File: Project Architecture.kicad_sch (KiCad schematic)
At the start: 0 parts

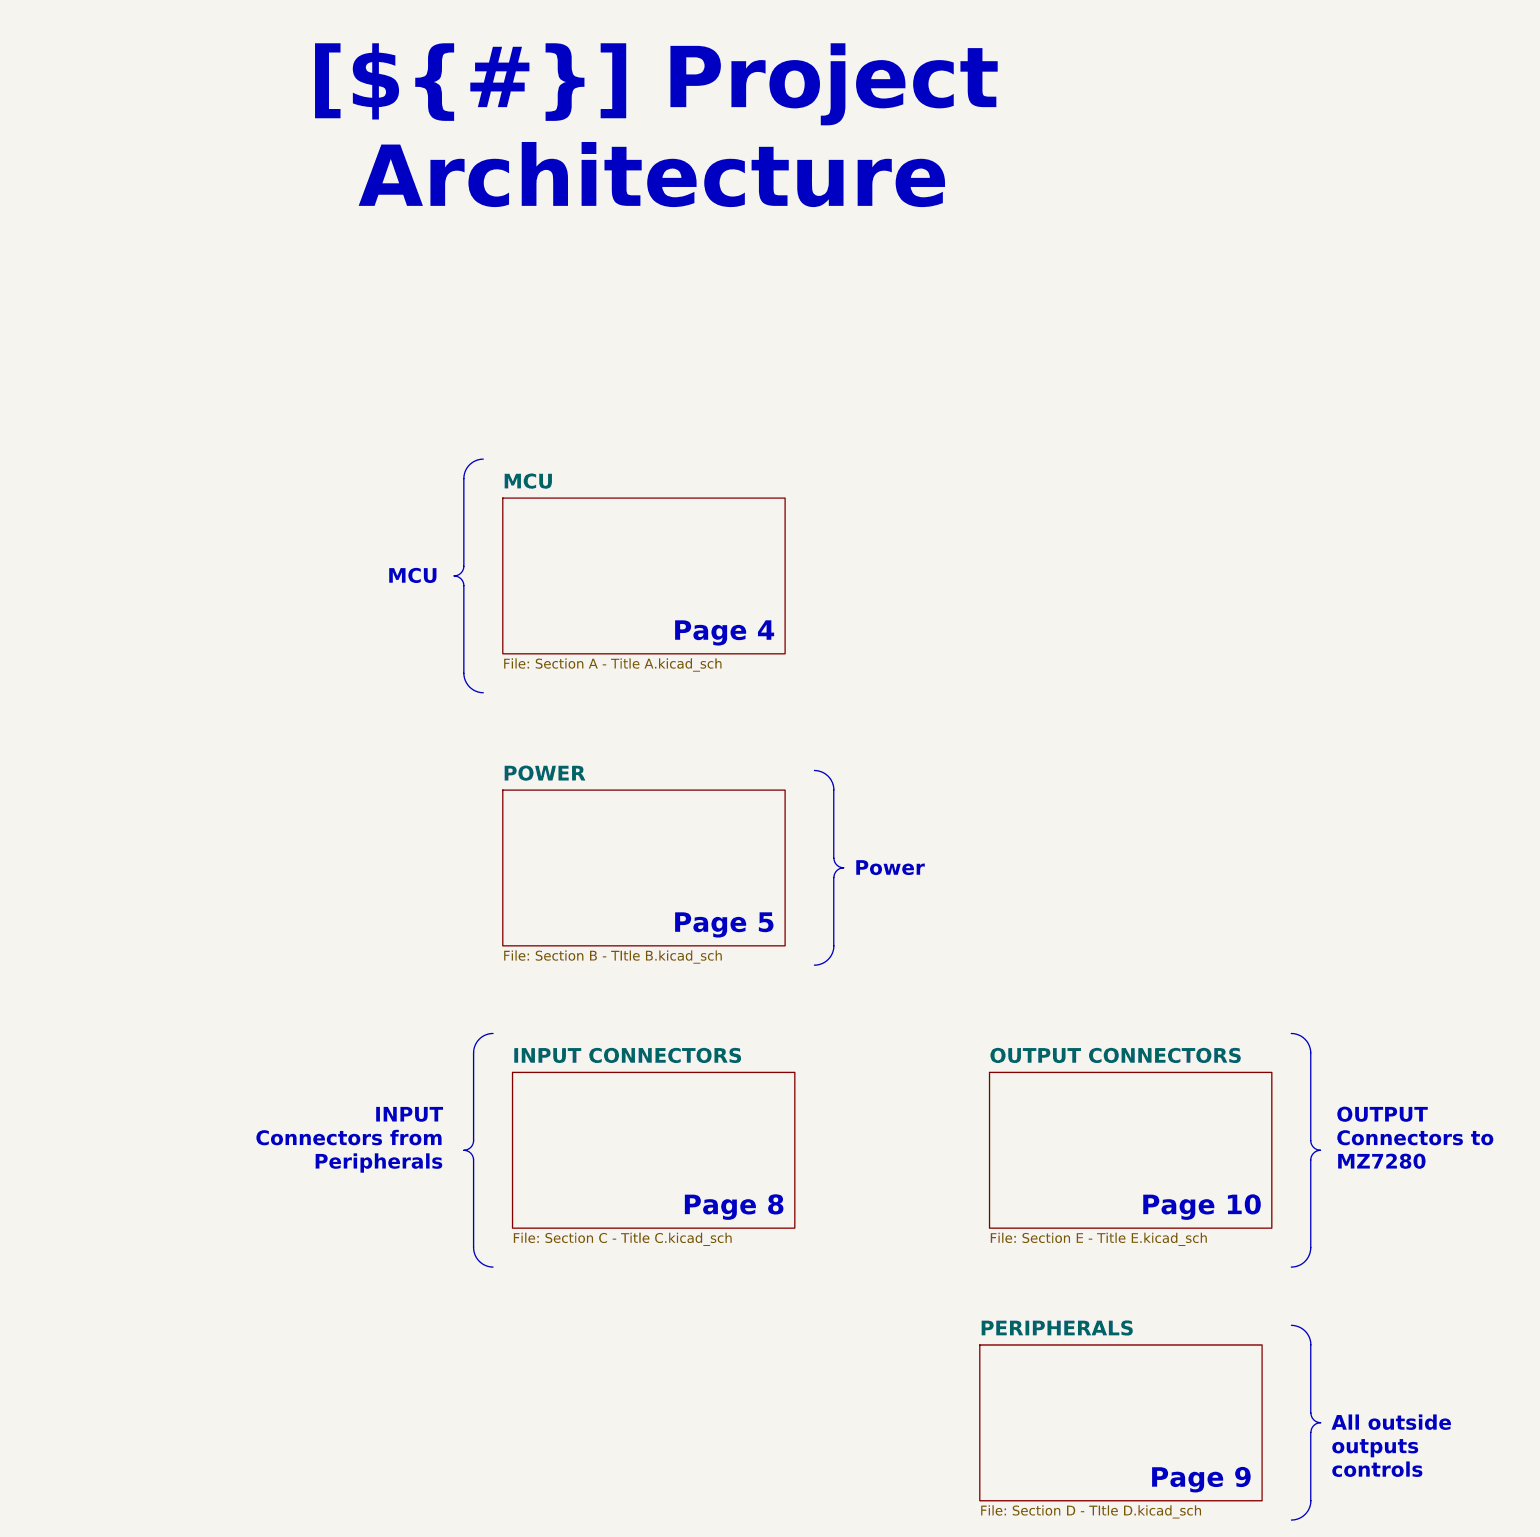
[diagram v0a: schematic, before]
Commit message: [SCHEMATICS] Ajout de convertisseur + autres
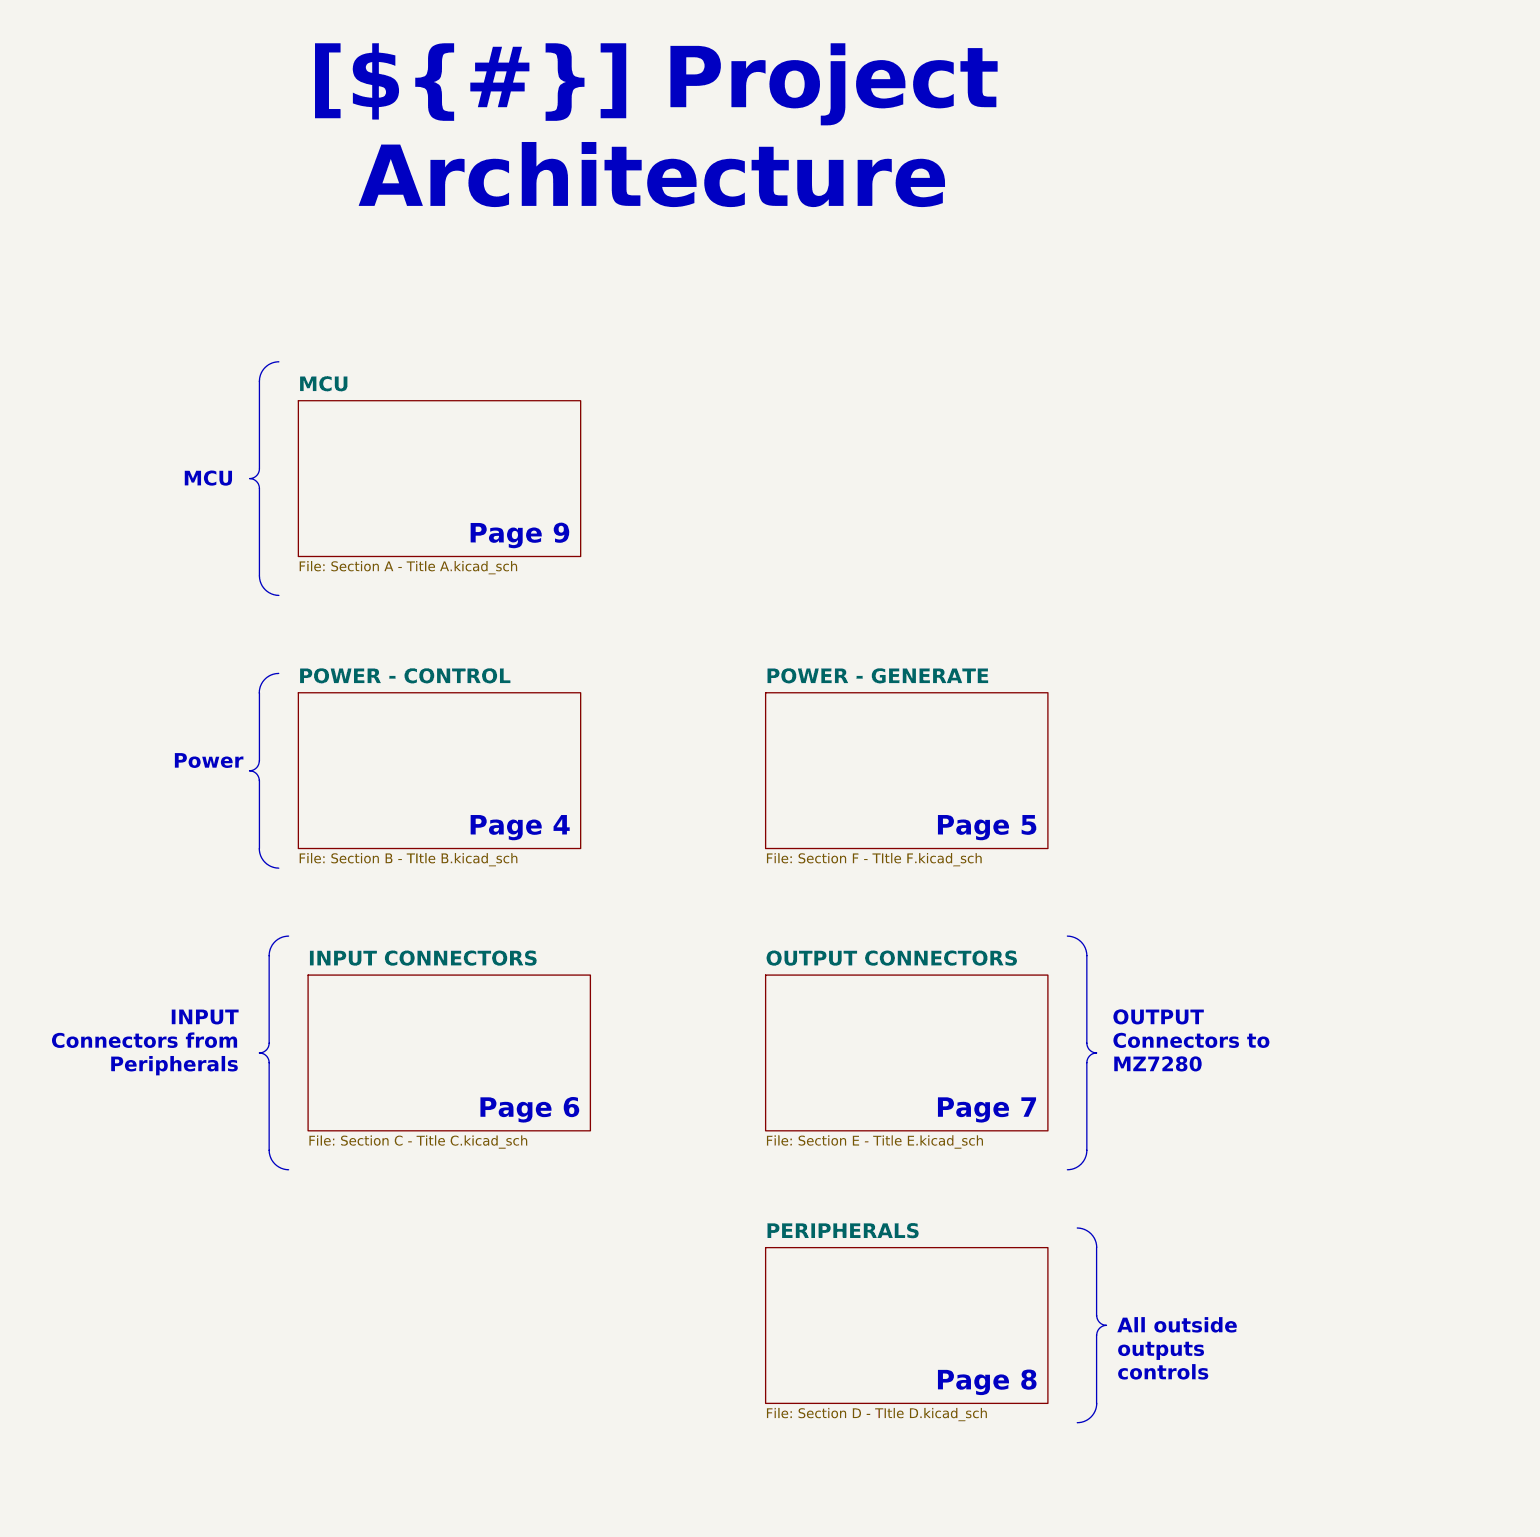
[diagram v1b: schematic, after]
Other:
- sheet POWER renamed POWER - CONTROL
- added sheet POWER - GENERATE (Section F - TItle F.kicad_sch)
- note added: "Page 6"
- note added: "Page 7"
- note removed: "Page 10"
